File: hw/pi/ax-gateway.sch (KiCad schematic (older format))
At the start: 92 parts, among them IC1 TG-5006CJ, IC2 TPS73433, IC3 AX5243, IC4 AX5243, P1 Raspberry_Pi_Conn, P2 COAX, P3 COAX, P4 PAD

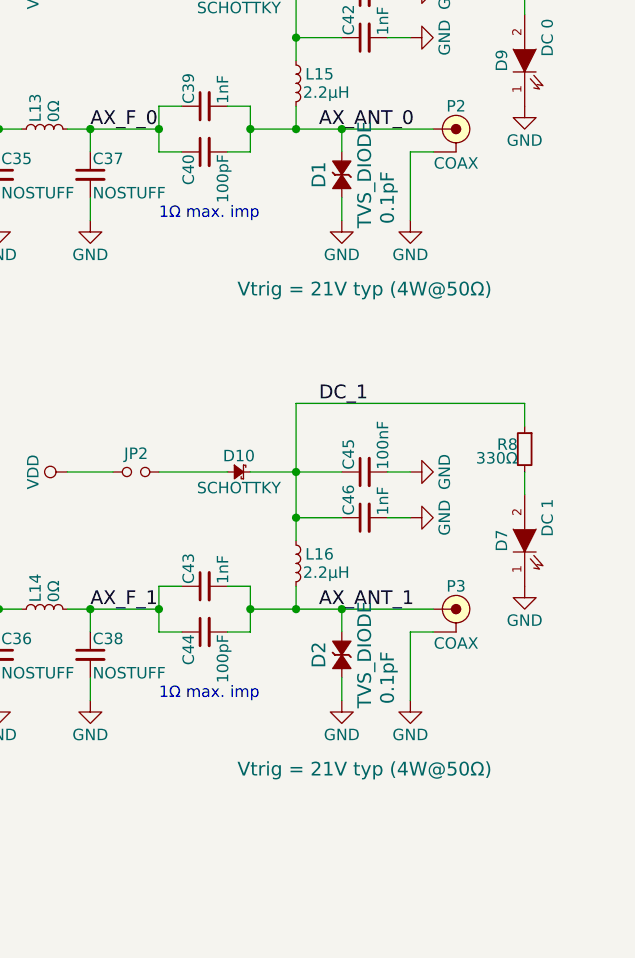
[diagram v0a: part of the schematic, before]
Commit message: [hw] tidy boms, regen artifacts, update READMEs
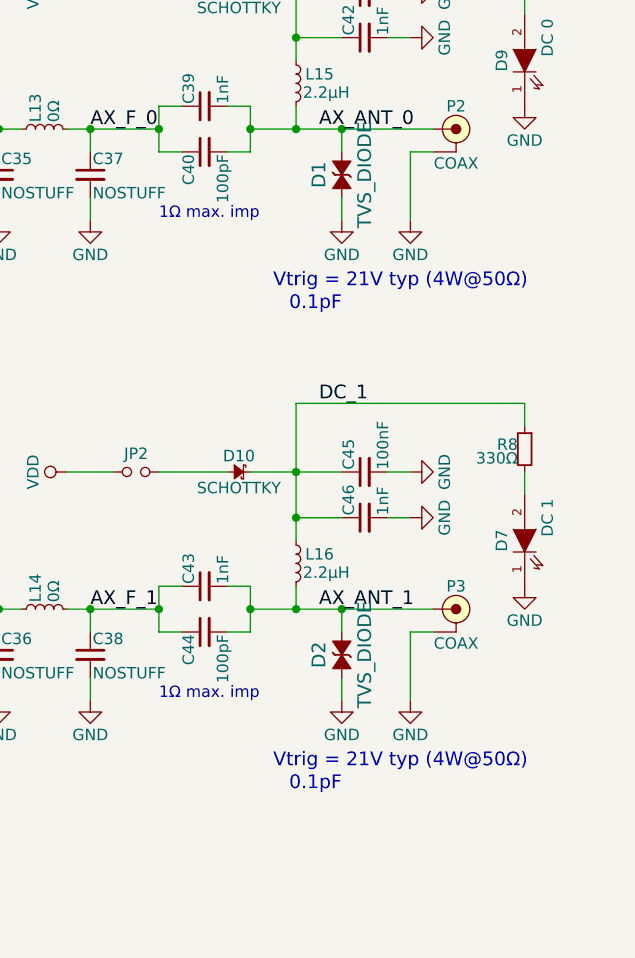
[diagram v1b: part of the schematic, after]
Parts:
- D1, D2: Capacitance 0.1pF -> (none); Vtrig Vtrig = 21V typ (4W@50Ω) -> (none)
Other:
- note added: "0.1pF"
- note added: "Vtrig = 21V typ (4W@50Ω)"
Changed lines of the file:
@@
 F 3 "http://www.farnell.com/datasheets/1992039.pdf" H 10300 1700 60  0001 C CNN
 F 4 "2480929" H 10200 1600 60  0001 C CNN "Farnell"
-F 5 "0.1pF" H 10400 1400 60  0000 C CNN "Capacitance"
-F 6 "Vtrig = 21V typ (4W@50Ω)" V 10800 1500 60  0000 C CNN "Vtrig"
 	1    10200 1600
 	0    -1   1    0
@@
 F 3 "http://www.farnell.com/datasheets/1992039.pdf" H 10300 3800 60  0001 C CNN
 F 4 "2480929" H 10200 3700 60  0001 C CNN "Farnell"
-F 5 "0.1pF" H 10400 3500 60  0000 C CNN "Capacitance"
-F 6 "Vtrig = 21V typ (4W@50Ω)" V 10800 3600 60  0000 C CNN "Vtrig"
 	1    10200 3700
 	0    -1   1    0
@@
 Text Label 5300 4800 0    60   ~ 0
 L2_1
+Text Notes 9900 2200 0    60   ~ 0
+Vtrig = 21V typ (4W@50Ω)
+Text Notes 10200 2300 2    60   ~ 0
+0.1pF
+Text Notes 9900 4300 0    60   ~ 0
+Vtrig = 21V typ (4W@50Ω)
+Text Notes 10200 4400 2    60   ~ 0
+0.1pF
 $EndSCHEMATC
